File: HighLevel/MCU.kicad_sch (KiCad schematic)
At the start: 1 part, among them U1 STM32F405RGTx

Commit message: Finish MCU
Updated MCU as per drawing
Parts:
- added C10, C11, C12, C13, C4, C5, C6, C7: 2.2u, symbol Device:C
- added C3, C9: 15p, symbol Device:C
- added C8: 100n, symbol Device:C
- added Y1: ~, symbol Device:Crystal_GND24
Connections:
- net at U1.1 (VBAT): now also U1.19 (VDD), U1.32 (VDD), U1.48 (VDD), U1.64 (VDD)
- net CURRENT_3: now reaches U1.10 (PC2)
- net AN_IN: now reaches U1.11 (PC3)
- net GND: now reaches U1.12 (VSSA)
- net GND: now also U1.18 (VSS), U1.60 (BOOT0), U1.63 (VSS), C13.2, C3.1, C4.2, C5.1, C6.2, C7.2, C8.2, C9.1, Y1.2, Y1.4
- net at U1.13 (VDDA): now also C6.1, C7.1
- net Voltage_2: now reaches U1.15 (PA1)
- net Voltage_3: now reaches U1.16 (PA2)
- net ADC_TEMP: now reaches U1.17 (PA3)
- net RX_SDA_NSS: now reaches U1.20 (PA4)
- net RX_SDA_NSS: now also U1.30 (PB11)
- net SCK_ADC_EXT: now reaches U1.21 (PA5)
- net MISO_ADC_EXT2: now reaches U1.22 (PA6)
- net TX_SCL_MOSI: now reaches U1.23 (PA7)
- net TEMP_MOTOR: now reaches U1.24 (PC4)
- net ADC_15: now reaches U1.25 (PC5)
- net ADC_TEMP2: now reaches U1.26 (PB0)
- net ADC_TEMP3: now reaches U1.27 (PB1)
- net TX_SCK_MOSI: now reaches U1.29 (PB10)
- net at U1.31 (VCAP_1): now also C4.1
- net L1: now reaches U1.34 (PB13)
- net L2: now reaches U1.35 (PB14)
- net L3: now reaches U1.36 (PB15)
- net HALL_1: now reaches U1.37 (PC6)
- net HALL_2: now reaches U1.38 (PC7)
- net HALL_3: now reaches U1.39 (PC8)
- net PC9: now reaches U1.40 (PC9)
- net H1: now reaches U1.41 (PA8)
- net H2: now reaches U1.42 (PA9)
- net H3: now reaches U1.43 (PA10)
- net USB_DM: now reaches U1.44 (PA11)
- net USB_DP: now reaches U1.45 (PA12)
- net SWDIO: now reaches U1.46 (PA13)
- net at U1.47 (VCAP_2): now also C5.2
- net SWCLK: now reaches U1.49 (PA14)
- net at U1.5 (PH0): now also C3.2, Y1.1
- net PC10_UART_TX: now reaches U1.51 (PC10)
- net PX11_UART_RX: now reaches U1.52 (PC11)
- net PC12: now reaches U1.53 (PC12)
- net CURR_FILTER: now reaches U1.54 (PD2)
- net LED_GREEN: now reaches U1.57 (PB5)
- net SERVO: now reaches U1.58 (PB6)
- net LED_RED: now reaches U1.59 (PB7)
- net at U1.6 (PH1): now also C9.2, Y1.3
- net CAN_RX: now reaches U1.61 (PB8)
- net CAN_TX: now reaches U1.62 (PB9)
- net NRST: now reaches U1.7 (NRST)
- net NRST: now also C8.1
- net CURRENT_1: now reaches U1.8 (PC0)
- net CURRENT_2: now reaches U1.9 (PC1)
- no-connect marks 0 -> 8

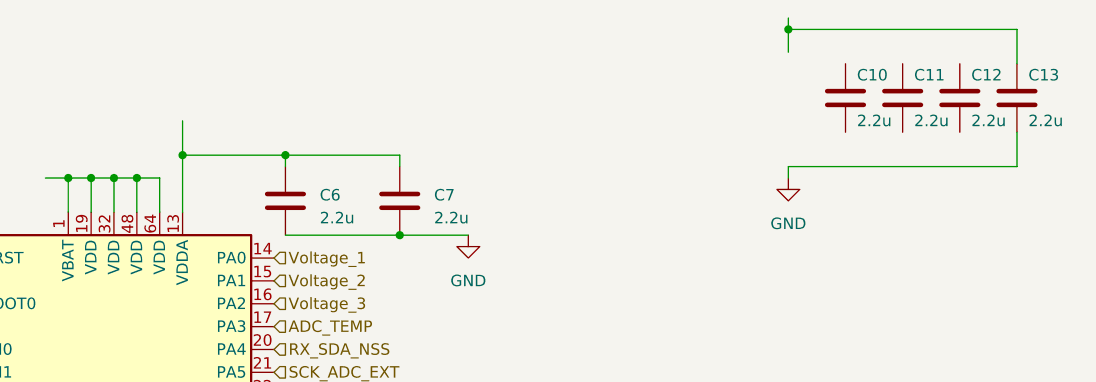
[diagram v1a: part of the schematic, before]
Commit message: Minor fixes
Fixed some wires that were not connected to capacitor
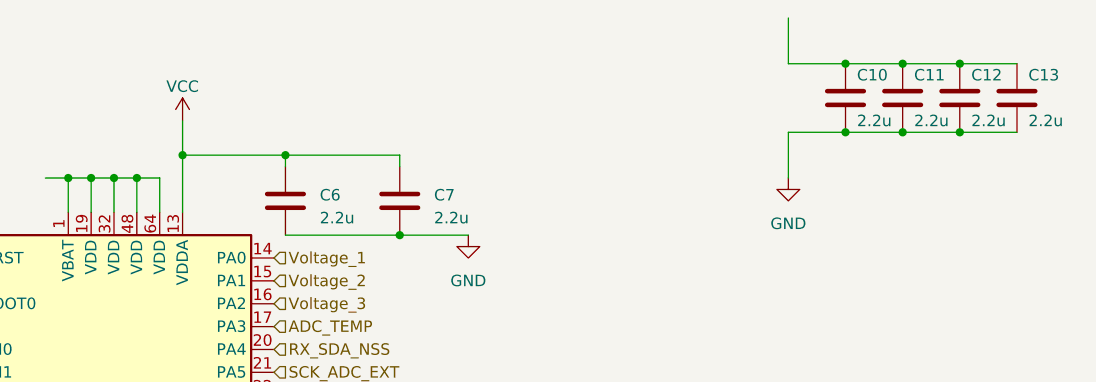
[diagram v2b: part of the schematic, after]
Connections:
- net GND: now also C10.2, C11.2, C12.2
- net at C12.1: now also C10.1, C11.1, C13.1
- net VCC: now reaches C6.1, C7.1, U1.13 (VDDA)
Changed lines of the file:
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@@
   (junction (at 173.99 36.83) (diameter 0) (color 0 0 0 0)
   )
+  (junction (at 252.73 31.75) (diameter 0) (color 0 0 0 0)
+  )
   (junction (at 130.81 62.23) (diameter 0) (color 0 0 0 0)
   )
+  (junction (at 259.08 31.75) (diameter 0) (color 0 0 0 0)
+  )
   (junction (at 179.07 34.29) (diameter 0) (color 0 0 0 0)
   )
@@
   (junction (at 190.5 34.29) (diameter 0) (color 0 0 0 0)
   )
+  (junction (at 259.08 24.13) (diameter 0) (color 0 0 0 0)
+  )
   (junction (at 121.92 55.88) (diameter 0) (color 0 0 0 0)
   )
@@
   (junction (at 168.91 36.83) (diameter 0) (color 0 0 0 0)
   )
+  (junction (at 265.43 24.13) (diameter 0) (color 0 0 0 0)
+  )
   (junction (at 121.92 48.26) (diameter 0) (color 0 0 0 0)
   )
-  (junction (at 246.38 20.32) (diameter 0) (color 0 0 0 0)
+  (junction (at 265.43 31.75) (diameter 0) (color 0 0 0 0)
   )
   (junction (at 127 125.73) (diameter 0) (color 0 0 0 0)
   )
   (junction (at 146.05 48.26) (diameter 0) (color 0 0 0 0)
+  )
+  (junction (at 252.73 24.13) (diameter 0) (color 0 0 0 0)
   )
   (no_connect (at 153.67 101.6))
@@
     (stroke (width 0) (type default))
   )
+  (wire (pts (xy 246.38 19.05) (xy 246.38 24.13))
+    (stroke (width 0) (type default))
+  )
   (wire (pts (xy 121.92 71.12) (xy 121.92 55.88))
     (stroke (width 0) (type default))
@@
     (stroke (width 0) (type default))
   )
-  (wire (pts (xy 271.78 31.75) (xy 271.78 35.56))
-    (stroke (width 0) (type default))
-  )
   (wire (pts (xy 146.05 55.88) (xy 153.67 55.88))
     (stroke (width 0) (type default))
   )
-  (wire (pts (xy 246.38 19.05) (xy 246.38 20.32))
-    (stroke (width 0) (type default))
-  )
   (wire (pts (xy 113.03 48.26) (xy 113.03 52.07))
     (stroke (width 0) (type default))
   )
-  (wire (pts (xy 246.38 20.32) (xy 246.38 22.86))
-    (stroke (width 0) (type default))
-  )
   (wire (pts (xy 179.07 40.64) (xy 179.07 34.29))
     (stroke (width 0) (type default))
   )
+  (wire (pts (xy 265.43 31.75) (xy 259.08 31.75))
+    (stroke (width 0) (type default))
+  )
   (wire (pts (xy 171.45 137.16) (xy 173.99 137.16))
     (stroke (width 0) (type default))
@@
     (stroke (width 0) (type default))
   )
+  (wire (pts (xy 252.73 24.13) (xy 259.08 24.13))
+    (stroke (width 0) (type default))
+  )
   (wire (pts (xy 139.7 114.3) (xy 139.7 125.73))
     (stroke (width 0) (type default))
@@
     (stroke (width 0) (type default))
   )
+  (wire (pts (xy 259.08 31.75) (xy 252.73 31.75))
+    (stroke (width 0) (type default))
+  )
   (wire (pts (xy 130.81 49.53) (xy 135.89 49.53))
     (stroke (width 0) (type default))
@@
     (stroke (width 0) (type default))
   )
+  (wire (pts (xy 265.43 24.13) (xy 271.78 24.13))
+    (stroke (width 0) (type default))
+  )
+  (wire (pts (xy 259.08 24.13) (xy 265.43 24.13))
+    (stroke (width 0) (type default))
+  )
   (wire (pts (xy 176.53 36.83) (xy 176.53 40.64))
     (stroke (width 0) (type default))
@@
     (stroke (width 0) (type default))
   )
-  (wire (pts (xy 246.38 20.32) (xy 271.78 20.32))
+  (wire (pts (xy 246.38 24.13) (xy 252.73 24.13))
     (stroke (width 0) (type default))
   )
@@
     (stroke (width 0) (type default))
   )
-  (wire (pts (xy 246.38 35.56) (xy 246.38 36.83))
+  (wire (pts (xy 246.38 31.75) (xy 246.38 36.83))
     (stroke (width 0) (type default))
   )
@@
     (stroke (width 0) (type default))
   )
+  (wire (pts (xy 252.73 31.75) (xy 246.38 31.75))
+    (stroke (width 0) (type default))
+  )
   (wire (pts (xy 127 115.57) (xy 127 125.73))
     (stroke (width 0) (type default))
@@
     (stroke (width 0) (type default))
   )
-  (wire (pts (xy 271.78 35.56) (xy 246.38 35.56))
+  (wire (pts (xy 271.78 31.75) (xy 265.43 31.75))
     (stroke (width 0) (type default))
   )
@@
   )
   (wire (pts (xy 173.99 134.62) (xy 173.99 137.16))
-    (stroke (width 0) (type default))
-  )
-  (wire (pts (xy 271.78 20.32) (xy 271.78 24.13))
     (stroke (width 0) (type default))
   )
@@
     )
   )
-  (netclass_flag "" (length 2.54) (shape round) (at 179.07 30.48 0) (fields_autoplaced)
-    (effects (font (size 1.27 1.27)) (justify left bottom))
-    (property "Netclass" "VCC" (at 179.7685 27.94 0)
-      (effects (font (size 1.27 1.27) italic) (justify left))
-    )
-  )
   (netclass_flag "" (length 2.54) (shape round) (at 246.38 19.05 0) (fields_autoplaced)
     (effects (font (size 1.27 1.27)) (justify left bottom))
@@
     )
   )
+  (symbol (lib_id "power:VCC") (at 179.07 30.48 0) (unit 1)
+    (in_bom yes) (on_board yes) (dnp no) (fields_autoplaced)
+    (property "Reference" "#PWR08" (at 179.07 34.29 0)
+      (effects (font (size 1.27 1.27)) hide)
+    )
+    (property "Value" "VCC" (at 179.07 26.67 0)
+      (effects (font (size 1.27 1.27)))
+    )
+    (property "Footprint" "" (at 179.07 30.48 0)
+      (effects (font (size 1.27 1.27)) hide)
+    )
+    (property "Datasheet" "" (at 179.07 30.48 0)
+      (effects (font (size 1.27 1.27)) hide)
+    )
+    (pin "1")
+    (instances
+      (project "MCU"
+        (path "/f67b84bb-fc24-4057-a4d1-5dd671e1b3ff"
+          (reference "#PWR08") (unit 1)
+        )
+      )
+    )
+  )
